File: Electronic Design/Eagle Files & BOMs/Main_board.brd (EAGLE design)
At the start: 100 x 63.5 mm, 43 parts, among them IC2 ATMEGA328-PU, IC3 LM2576S, Q1 IRF9540, Q2 IRF9540, X1 16MHz

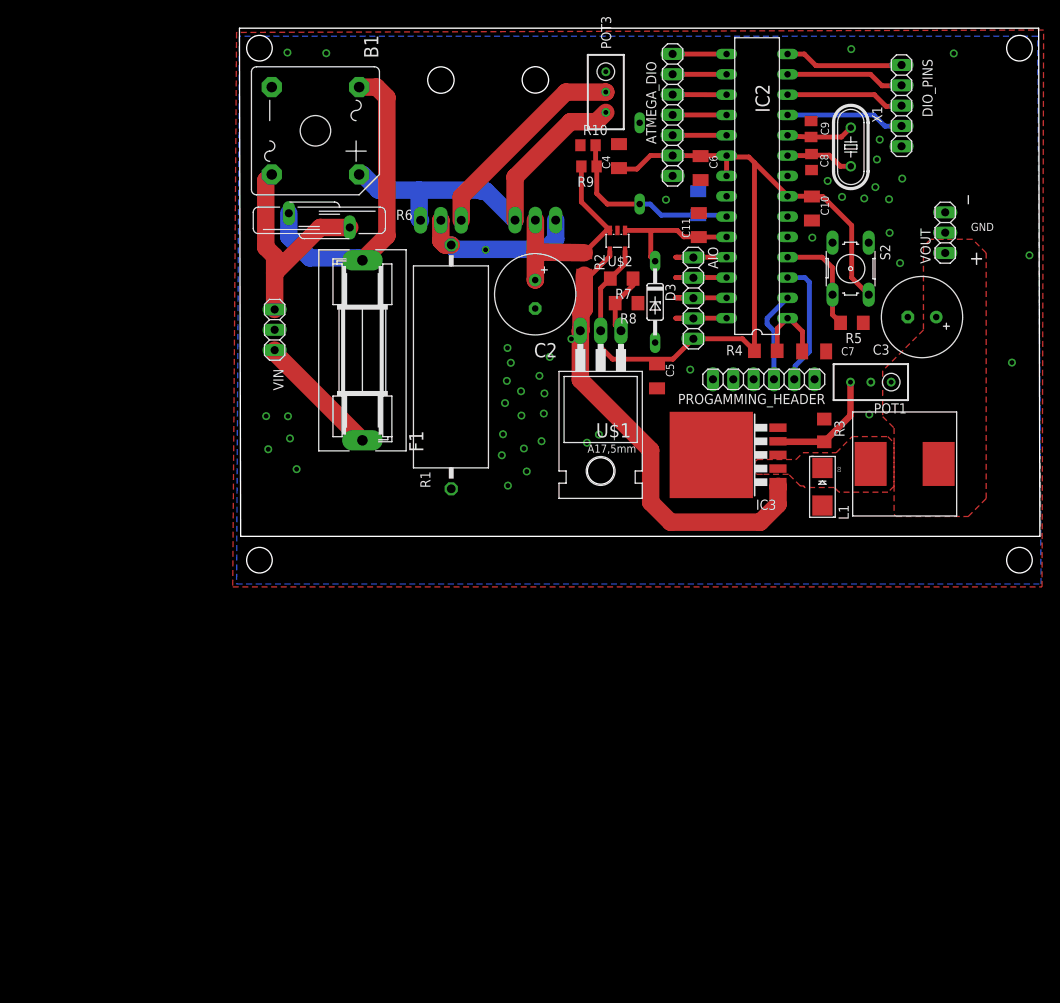
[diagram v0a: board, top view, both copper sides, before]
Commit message: adding ground to AIO and general tidy up
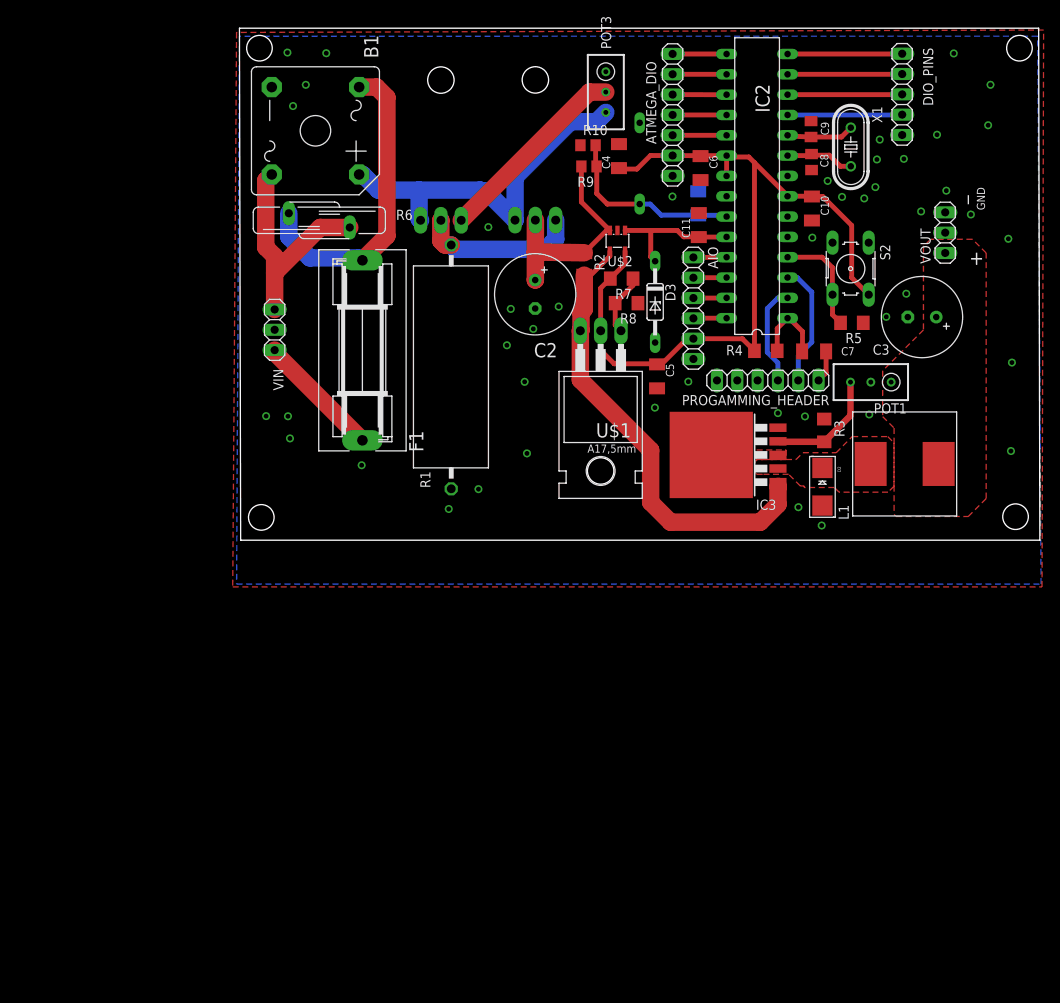
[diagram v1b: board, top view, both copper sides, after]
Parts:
- AIO: device pinhead:1X05 -> pinhead:1X06
- moved DIO_PINS 1.41 mm to (82.8, 60.7)
- moved AIO 1.26 mm to (56.7, 34.0)
- moved PROGAMMING_HEADER 0.52 mm to (66.0, 25.0)
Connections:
- net GND: now also AIO.6
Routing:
- net ANALOG_5: track 8.55 -> 4.16 mm
- net ANALOG_4: track 8.55 -> 4.16 mm
- net ANALOG_3: track 8.55 -> 4.16 mm
- net ANALOG_2: track 8.55 -> 4.16 mm
- net N$14: track 0.00 -> 4.02 mm
- net N$7: track 26.4 -> 24.7 mm
- net N$5: track 11.6 -> 12.6 mm
- net +5V: track 104.0 -> 104.8 mm
- net N$22: track 14.9 -> 14.3 mm
- net N$20: track 14.9 -> 14.3 mm
- net N$21: track 14.9 -> 14.3 mm
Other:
- board size 100 x 63.5 mm -> 100 x 64 mm

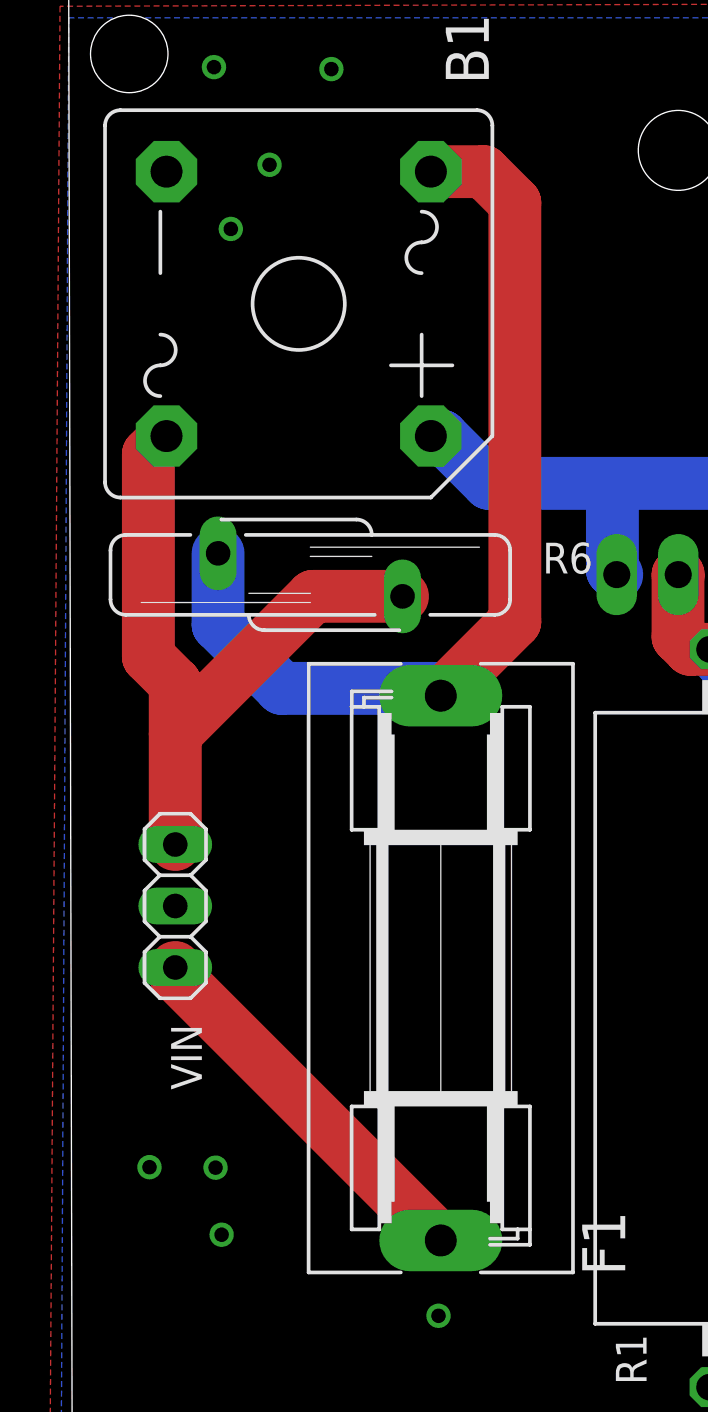
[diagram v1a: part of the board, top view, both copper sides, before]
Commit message: Moving fuse close to output rather than input
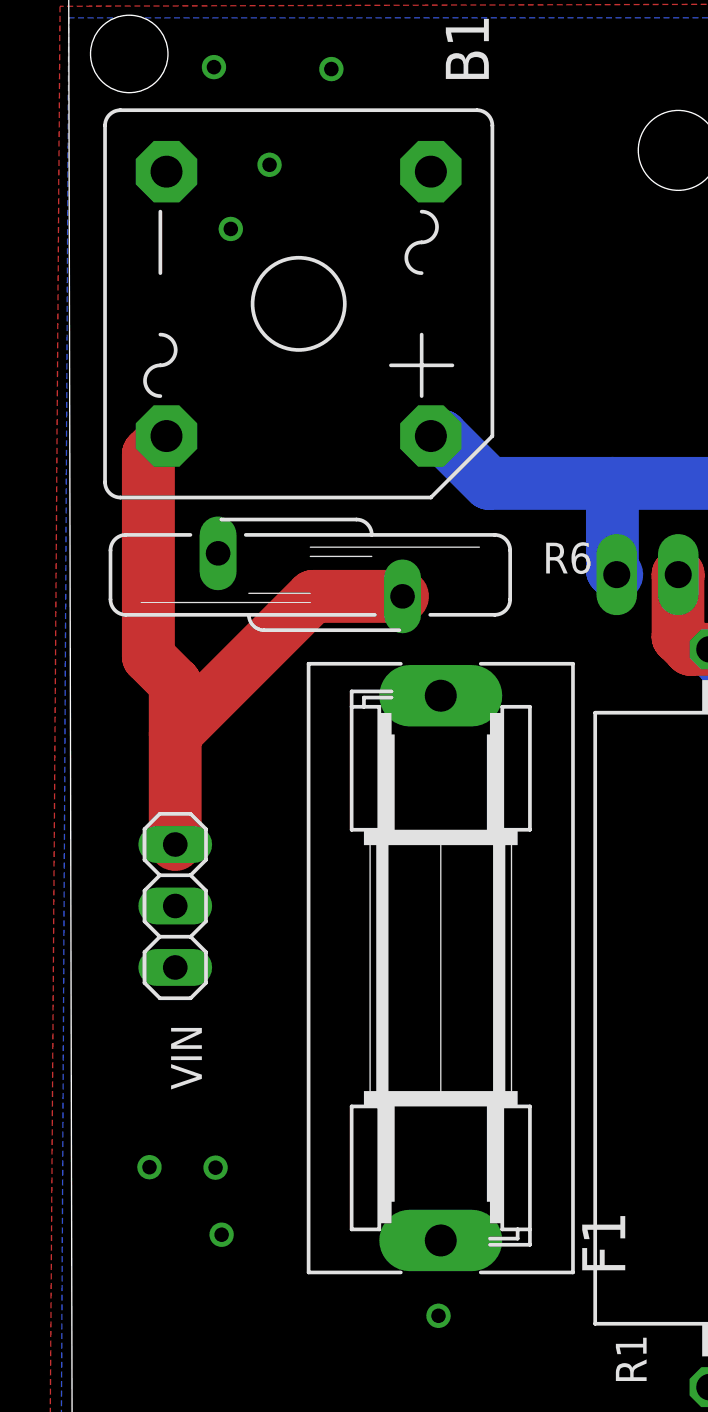
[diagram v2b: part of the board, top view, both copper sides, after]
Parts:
- R10: value 21k5 -> 1k13
- R9: value 1k13 -> 21k5
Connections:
- removed net N$18: B1.AC1, F1.2, R6.1
- new net N$2: F1.2, VOUT.1
- net N$1: now also B1.AC1, R6.1; no longer F1.1
- net N$24: now also F1.1; no longer VOUT.1
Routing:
- net N$18: track 39.0 -> 0.00 mm
- net N$1: track 15.8 -> 0.00 mm
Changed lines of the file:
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@@
 <element name="C11" library="resistor" package="C1206K" value="10n" x="57.42" y="44.39" rot="R90"/>
 <element name="D3" library="diode" package="DO35Z10" value="5.1V" x="51.96" y="34.79" rot="R270"/>
-<element name="R9" library="resistor" package="R0805" value="1k13" x="43.69" y="51.72" rot="R180"/>
-<element name="R10" library="resistor" package="R0805" value="21k5" x="43.57" y="54.37"/>
+<element name="R9" library="resistor" package="R0805" value="21k5" x="43.69" y="51.72" rot="R180"/>
+<element name="R10" library="resistor" package="R0805" value="1k13" x="43.57" y="54.37"/>
 </elements>
 <signals>
@@
 <wire x1="10.091" y1="44.091" x2="4.4" y2="38.4" width="2.1844" layer="1"/>
 </signal>
-<signal name="N$1">
-<contactref element="VIN" pad="3"/>
-<contactref element="F1" pad="1"/>
-<wire x1="4.4" y1="28.76" x2="4.4" y2="28.45221875" width="2.1844" layer="1"/>
-<wire x1="4.4" y1="28.45221875" x2="15.370003125" y2="17.482215625" width="2.1844" layer="1"/>
-</signal>
-<signal name="N$18">
-<contactref element="F1" pad="2"/>
-<contactref element="R6" pad="1"/>
-<contactref element="B1" pad="AC1"/>
-<wire x1="14.960996875" y1="61.636584375" x2="17.143415625" y2="61.636584375" width="2.1844" layer="1"/>
-<wire x1="17.143415625" y1="61.636584375" x2="18.43" y2="60.35" width="2.1844" layer="1"/>
-<wire x1="18.43" y1="60.35" x2="18.43" y2="43.0466125" width="2.1844" layer="1"/>
-<wire x1="18.43" y1="43.0466125" x2="15.370003125" y2="39.986615625" width="2.1844" layer="1"/>
-<wire x1="6.17" y1="45.869" x2="6.17" y2="42.92" width="2.1844" layer="16"/>
-<wire x1="6.17" y1="42.92" x2="8.8" y2="40.29" width="2.1844" layer="16"/>
-<wire x1="8.8" y1="40.29" x2="15.06661875" y2="40.29" width="2.1844" layer="16"/>
-<wire x1="15.06661875" y1="40.29" x2="15.370003125" y2="39.986615625" width="2.1844" layer="16"/>
-</signal>
 <signal name="ANALOG_3">
 <contactref element="IC2" pad="26"/>
@@
 <contactref element="POT1" pad="1"/>
 <contactref element="C3" pad="+"/>
-<contactref element="VOUT" pad="1"/>
 <polygon width="0.4064" layer="1" rank="3">
 <vertex x="82.09" y="7.96"/>
@@
 <vertex x="81.83" y="8.22"/>
 </polygon>
+<contactref element="F1" pad="1"/>
+<wire x1="81.46" y1="24.76" x2="87.098" y2="32.89" width="0" layer="19" extent="1-1"/>
+<wire x1="87.4" y1="14.53" x2="81.46" y2="24.76" width="0" layer="19" extent="1-1"/>
+<wire x1="15.370003125" y1="17.482215625" x2="81.46" y2="24.76" width="0" layer="19" extent="1-1"/>
 </signal>
 <signal name="N$26">
@@
 <wire x1="74.135715625" y1="33.175565625" x2="75.135740625" y2="32.175540625" width="0.6096" layer="1"/>
 </signal>
+<signal name="N$1">
+<contactref element="VIN" pad="3"/>
+<contactref element="R6" pad="1"/>
+<contactref element="B1" pad="AC1"/>
+<wire x1="6.17" y1="45.869" x2="14.960996875" y2="61.636584375" width="0" layer="19" extent="1-1"/>
+<wire x1="4.4" y1="28.76" x2="6.17" y2="45.869" width="0" layer="19" extent="1-1"/>
+</signal>
+<signal name="N$2">
+<contactref element="F1" pad="2"/>
+<contactref element="VOUT" pad="1"/>
+<wire x1="15.370003125" y1="39.986615625" x2="88.22" y2="40.9" width="0" layer="19" extent="1-1"/>
+</signal>
 </signals>

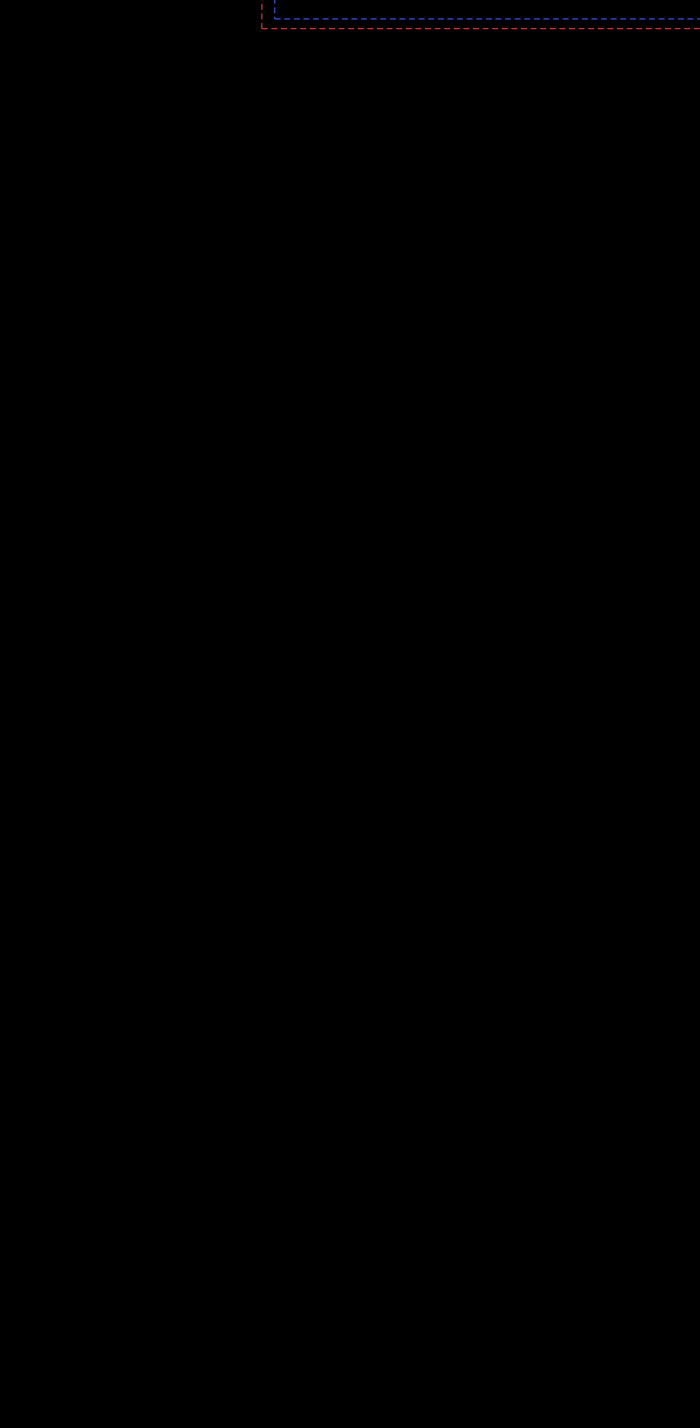
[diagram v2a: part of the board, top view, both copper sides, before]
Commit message: adding 5.1v zeners and LEDs to outputs of voltage regulators
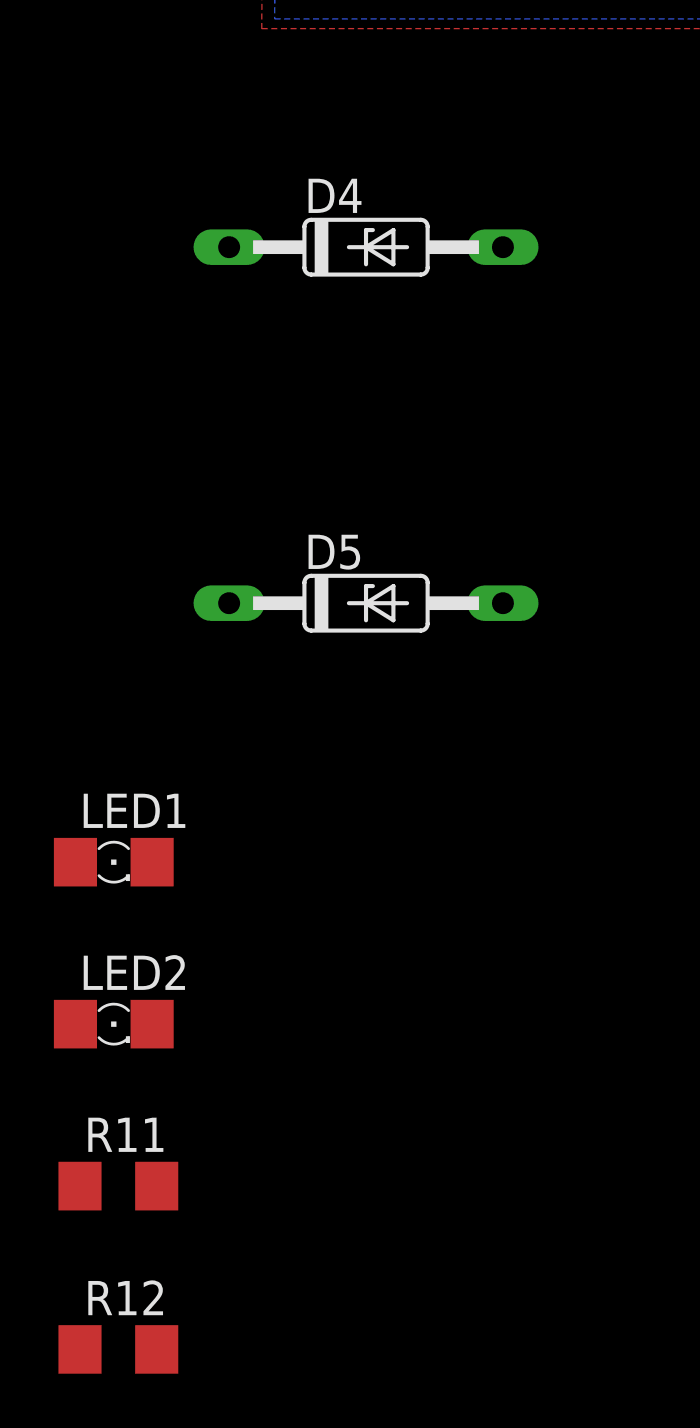
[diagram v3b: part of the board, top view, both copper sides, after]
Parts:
- added D4, D5: 5.1V, diode:DO35Z10
- added LED1, LED2: (no value), adafruit:1206
- added R11, R12: 2k, resistor:R1206
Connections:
- new net N$18: LED2.A, R11.1
- new net N$28: LED1.C, R12.2
- net +5V: now also D4.C, LED1.A
- net GND: now also D4.A, D5.A, LED2.C, R12.1
- net N$2: now also F1.1, L1.P$2, POT1.1; no longer F1.2, VOUT.1
- net N$24: now also D5.C, F1.2, R11.2, VOUT.1; no longer F1.1, L1.P$2, POT1.1
